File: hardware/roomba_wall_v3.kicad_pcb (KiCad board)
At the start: 2 copper layers, 27.9 x 26.7 mm, 15 parts, among them CON1 AVR-ISP-6, Q1 Q_NPN_BEC, SW1 Button, SW2 On/Off, U1 ATTINY45-20SU, Y1 8Mhz

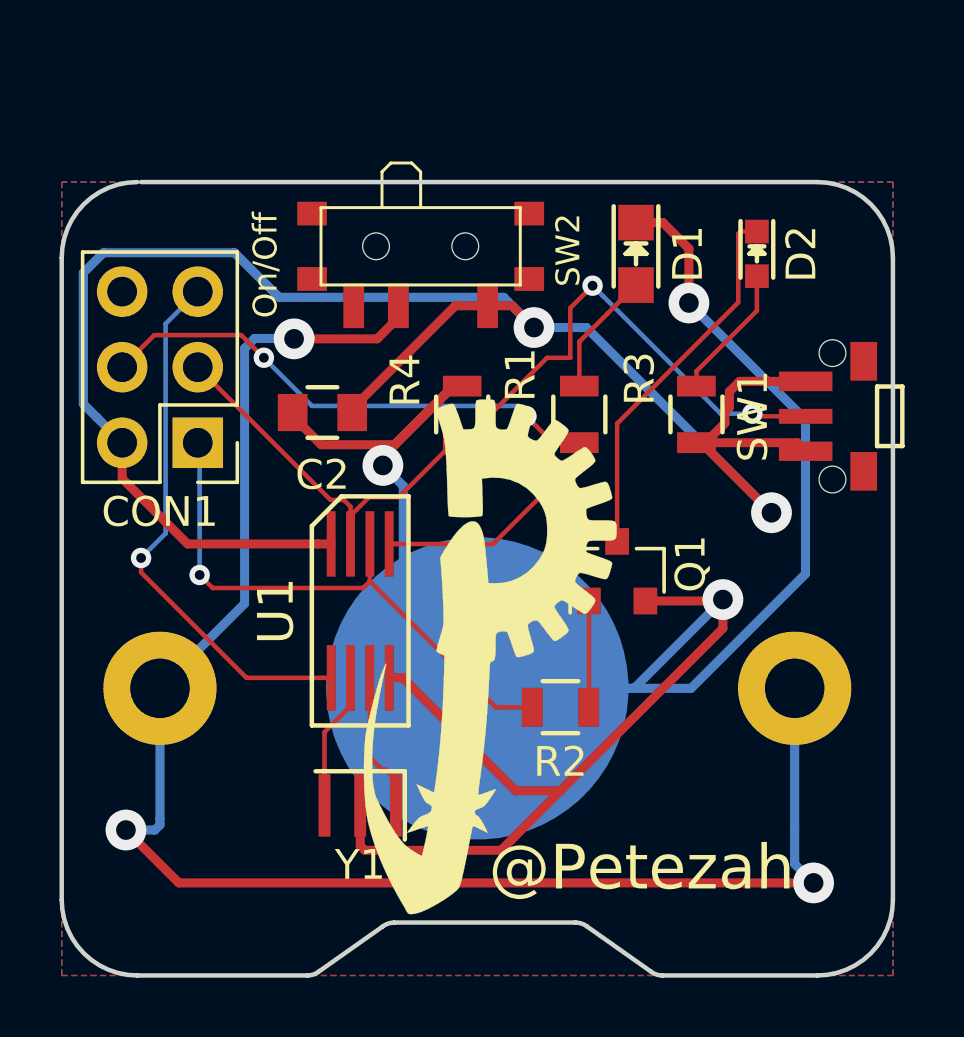
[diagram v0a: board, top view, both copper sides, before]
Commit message: Added a mounting hole for hanging and finalized layout for rev A Also exported gerbers
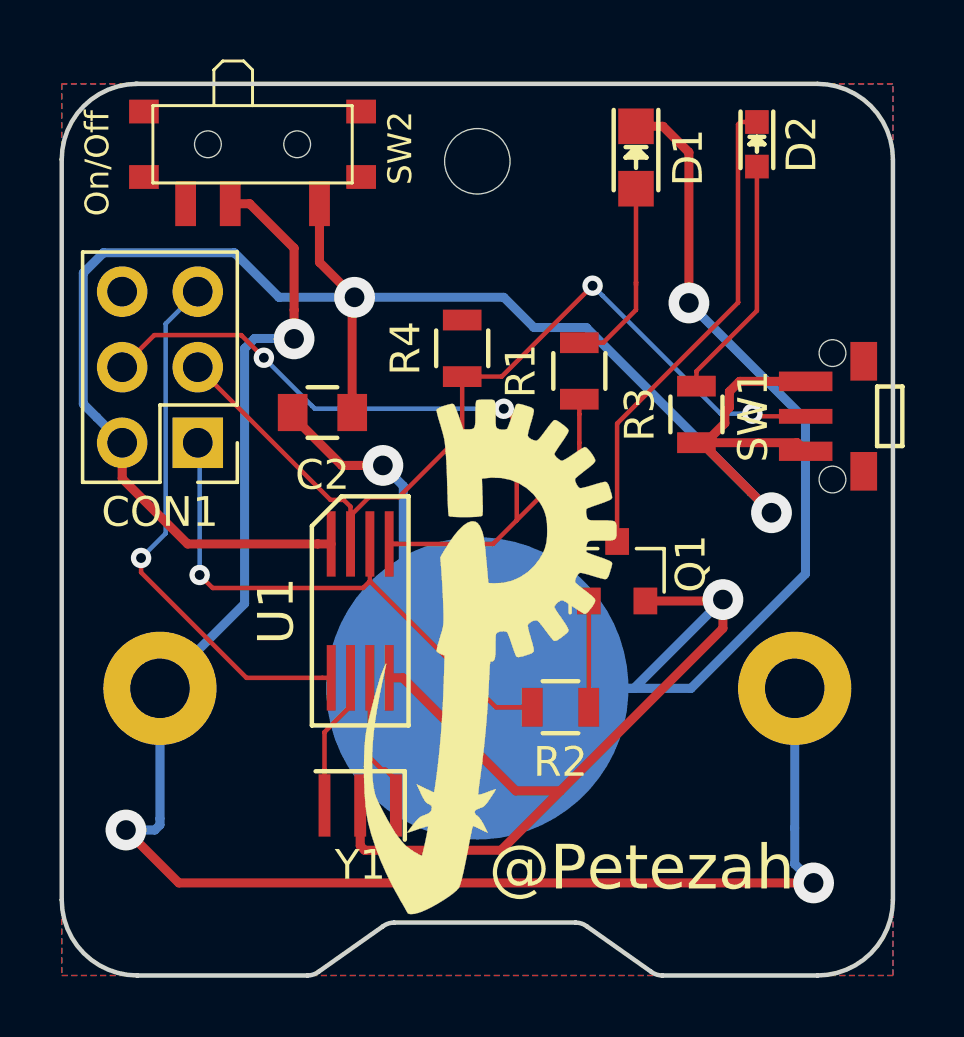
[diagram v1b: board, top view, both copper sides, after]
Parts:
- added REF**: MountingHole_2.2mm_M2, lib_fp:MountingHole_2.2mm_M2, F.Cu at (160.0, 107.3)
- moved SW2 6.61 mm to (152.5, 106.7)
- moved D2 3.68 mm to (169.4, 106.7)
- moved D1 3.24 mm to (165.4, 107.1)
- moved R4 2.22 mm to (159.5, 113.5)
- moved R1 1.46 mm to (163.4, 114.3)
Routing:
- net Net-(D2-Pad1): track 12.7 -> 16.4 mm
- net Net-(D2-Pad2): track 4.54 -> 8.22 mm
- net GND: track 83.9 -> 80.6 mm
- net Net-(D1-Pad2): track 4.19 -> 6.53 mm
- net /MOSI/INDICATOR: track 26.0 -> 28.1 mm
- net VBAT: track 55.1 -> 56.7 mm
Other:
- board size 27.9 x 26.7 mm -> 27.9 x 30 mm

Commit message: Working on rev B
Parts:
- removed SW2: On/Off, lib_fp:SSSS810701
- added G***: LOGO, kicad-libs:petezah-logo-xtiny, B.Cu at (148.1, 116.6)
- D2: footprint lib_fp:LED_0603 -> kicad-libs:VSMB3940X01-GS08
- moved CON1 9.12 mm to (155.0, 108.7), turned to 270 degrees
- moved D2 1.85 mm to (169.9, 108.5)
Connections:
- BT1 pad 1: VBAT -> +3V3
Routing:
- net GND: track 80.6 -> 1.03 mm, vias 3 -> 0
- net VBAT: track 56.7 -> 0.00 mm, vias 3 -> 0
- net +3V3: track 62.2 -> 39.2 mm, vias 2 -> 0
- net /RST: track 18.1 -> 32.0 mm, vias 1 -> 2
- net /MISO/IR: track 18.9 -> 27.0 mm
- net /MOSI/INDICATOR: track 28.1 -> 21.4 mm, vias 2 -> 1
- net Net-(D2-Pad2): track 8.22 -> 6.17 mm
- net Net-(D1-Pad2): track 6.53 -> 8.22 mm, vias 0 -> 2
- net Net-(D2-Pad1): track 16.4 -> 15.5 mm, vias 0 -> 2
- net /SCK/BUTTON: track 30.7 -> 31.6 mm
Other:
- net class 3V3: clearance 0.3048 -> 0.1524
- rule pad_to_mask_clearance: 0.2 -> 0.0508
- board text added: "Roomba Wall v3, Rev B (C) Copyright 2018 Peter Dunshee @Petezah"
- board text removed: "Roomba Wall v3, Rev A (C) Copyright 2018 Peter Dunshee @Petezah"

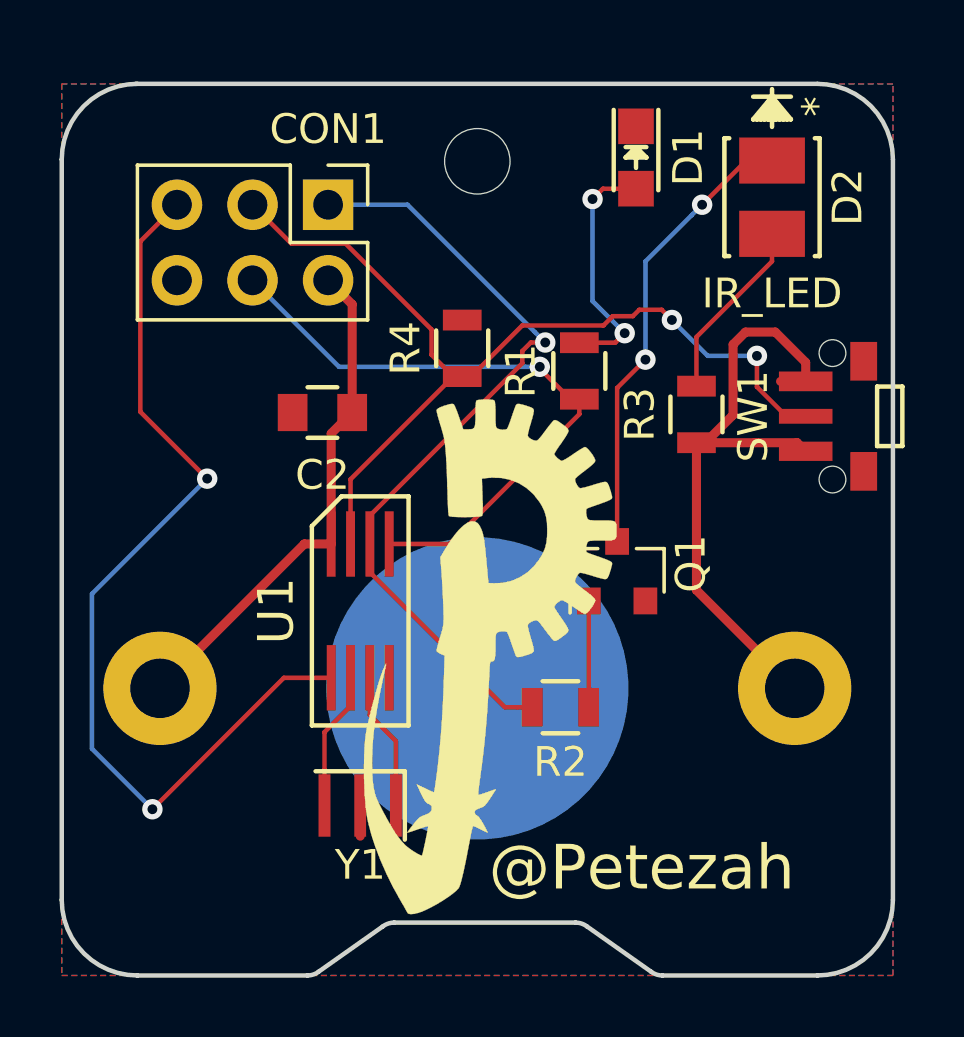
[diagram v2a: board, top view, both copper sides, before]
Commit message: Finished rev-b layout Updated gerbers Updated BOM Updated footprint archive Updated PDF schematic plot
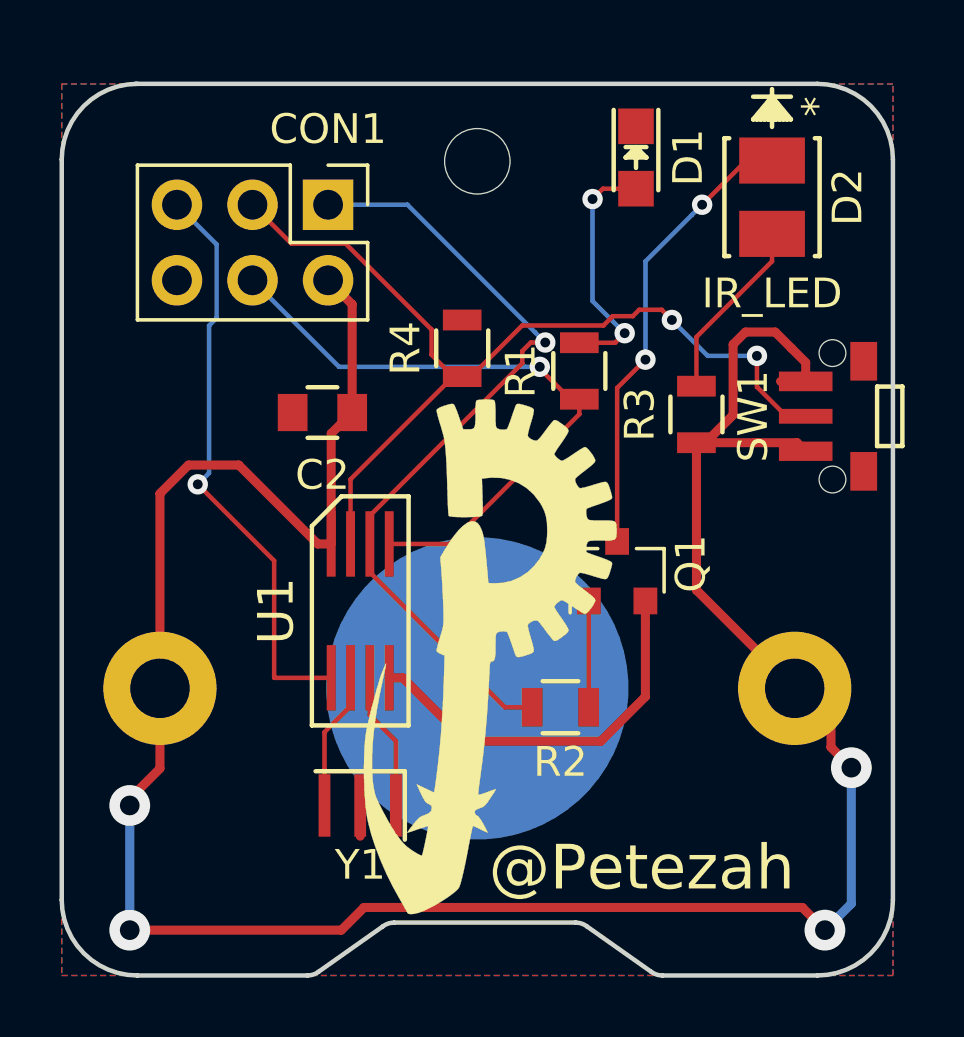
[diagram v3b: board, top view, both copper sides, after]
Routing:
- net +3V3: track 39.2 -> 87.0 mm, vias 0 -> 4
- net GND: track 1.03 -> 14.4 mm
- net /RST: track 32.0 -> 19.7 mm, vias 2 -> 1
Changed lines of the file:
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@@
-(kicad_pcb (version 4) (host pcbnew 4.0.6)
+(kicad_pcb (version 4) (host pcbnew 4.0.7)
   (general
     (links 28)
-    (no_connects 2)
-    (area 145.974999 104.572999 174.065001 134.695001)
+    (no_connects 0)
+    (area 144.267672 103.1241 176.2874 134.835901)
     (thickness 1.6)
     (drawings 18)
-    (tracks 106)
+    (tracks 134)
     (zones 0)
     (modules 16)
@@
   (gr_arc (start 148.59 132.08) (end 148.59 134.62) (angle 90) (layer Edge.Cuts) (width 0.15))
   (gr_arc (start 171.45 132.08) (end 173.99 132.08) (angle 90) (layer Edge.Cuts) (width 0.15))
+  (segment (start 159.766 126.746) (end 164.169642 126.746) (width 0.3048) (layer F.Cu) (net 1))
+  (segment (start 164.169642 126.746) (end 165.669 125.246642) (width 0.3048) (layer F.Cu) (net 1))
+  (segment (start 159.577801 126.557801) (end 159.766 126.746) (width 0.3048) (layer F.Cu) (net 1))
+  (segment (start 159.456101 126.557801) (end 159.577801 126.557801) (width 0.3048) (layer F.Cu) (net 1))
+  (segment (start 157.058 124.6145) (end 157.5128 124.6145) (width 0.3048) (layer F.Cu) (net 1))
+  (segment (start 157.5128 124.6145) (end 159.456101 126.557801) (width 0.3048) (layer F.Cu) (net 1))
+  (segment (start 165.669 122.7858) (end 165.669 122.031) (width 0.3048) (layer F.Cu) (net 1))
+  (segment (start 165.669 125.246642) (end 165.669 122.7858) (width 0.3048) (layer F.Cu) (net 1))
   (segment (start 156.083 129.938367) (end 156.083 128.905) (width 0.3048) (layer F.Cu) (net 1))
+  (segment (start 172.593 127.635) (end 171.907201 126.949201) (width 0.3048) (layer F.Cu) (net 2))
+  (segment (start 171.907201 126.949201) (end 171.907201 126.187201) (width 0.3048) (layer F.Cu) (net 2))
+  (segment (start 171.907201 126.187201) (end 170.688 124.968) (width 0.3048) (layer F.Cu) (net 2))
+  (segment (start 171.704 133.096) (end 172.593 132.207) (width 0.3048) (layer B.Cu) (net 2))
+  (segment (start 172.593 132.207) (end 172.593 127.635) (width 0.3048) (layer B.Cu) (net 2))
+  (via (at 172.593 127.635) (size 1.3716) (drill 0.6604) (layers F.Cu B.Cu) (net 2))
+  (segment (start 156.21 132.334) (end 170.942 132.334) (width 0.3048) (layer F.Cu) (net 2))
+  (segment (start 170.942 132.334) (end 171.704 133.096) (width 0.3048) (layer F.Cu) (net 2))
+  (via (at 171.704 133.096) (size 1.3716) (drill 0.6604) (layers F.Cu B.Cu) (net 2))
+  (segment (start 155.448 133.096) (end 156.21 132.334) (width 0.3048) (layer F.Cu) (net 2))
+  (segment (start 148.336 133.096) (end 155.448 133.096) (width 0.3048) (layer F.Cu) (net 2))
+  (segment (start 148.336 128.905) (end 148.336 133.096) (width 0.3048) (layer B.Cu) (net 2))
+  (via (at 148.336 133.096) (size 1.3716) (drill 0.6604) (layers F.Cu B.Cu) (net 2))
+  (segment (start 149.352 124.968) (end 149.352 127.662076) (width 0.3048) (layer F.Cu) (net 2))
+  (segment (start 149.352 127.662076) (end 148.336 128.678076) (width 0.3048) (layer F.Cu) (net 2))
+  (segment (start 148.336 128.678076) (end 148.336 128.905) (width 0.3048) (layer F.Cu) (net 2))
+  (via (at 148.336 128.905) (size 1.3716) (drill 0.6604) (layers F.Cu B.Cu) (net 2))
+  (segment (start 152.000998 117.462298) (end 154.6532 120.1145) (width 0.3048) (layer F.Cu) (net 2))
+  (segment (start 154.6532 120.1145) (end 155.108 120.1145) (width 0.3048) (layer F.Cu) (net 2))
+  (segment (start 150.311102 117.462298) (end 152.000998 117.462298) (width 0.3048) (layer F.Cu) (net 2))
+  (segment (start 149.352 118.4214) (end 150.311102 117.462298) (width 0.3048) (layer F.Cu) (net 2))
+  (segment (start 149.352 124.968) (end 149.352 118.4214) (width 0.3048) (layer F.Cu) (net 2))
+  (segment (start 171.058 114.0142) (end 170.5818 113.538) (width 0.3048) (layer F.Cu) (net 2))
+  (segment (start 170.5818 113.538) (end 170.035698 112.991898) (width 0.3048) (layer F.Cu) (net 2))
   (segment (start 168.617898 115.778602) (end 167.686 116.7105) (width 0.3048) (layer F.Cu) (net 2))
   (segment (start 167.686 116.7105) (end 167.386 116.7105) (width 0.3048) (layer F.Cu) (net 2))
@@
   (segment (start 169.3545 116.7105) (end 170.7695 116.7105) (width 0.3048) (layer F.Cu) (net 2))
   (segment (start 169.03395 112.991898) (end 168.617898 113.40795) (width 0.3048) (layer F.Cu) (net 2))
-  (segment (start 171.058 114.0142) (end 170.035698 112.991898) (width 0.3048) (layer F.Cu) (net 2))
   (segment (start 170.035698 112.991898) (end 169.03395 112.991898) (width 0.3048) (layer F.Cu) (net 2))
   (segment (start 171.058 114.649) (end 171.058 114.0142) (width 0.3048) (layer F.Cu) (net 2))
@@
   (segment (start 155.108 120.1145) (end 155.108 116.402) (width 0.3048) (layer F.Cu) (net 2))
   (segment (start 155.108 116.402) (end 155.813 115.697) (width 0.3048) (layer F.Cu) (net 2))
-  (segment (start 149.352 124.968) (end 154.2055 120.1145) (width 0.3048) (layer F.Cu) (net 2))
-  (segment (start 154.2055 120.1145) (end 155.108 120.1145) (width 0.3048) (layer F.Cu) (net 2))
   (segment (start 156.408 119.1645) (end 161.531311 114.041189) (width 0.1524) (layer F.Cu) (net 3))
   (segment (start 161.960789 113.00001) (end 162.303688 113.342909) (width 0.1524) (layer B.Cu) (net 3))
@@
   (segment (start 159.0869 120.1145) (end 163.449 115.7524) (width 0.1524) (layer F.Cu) (net 4))
   (segment (start 163.449 115.7524) (end 163.449 115.25) (width 0.1524) (layer F.Cu) (net 4))
-  (segment (start 149.098 129.032) (end 153.5155 124.6145) (width 0.1524) (layer F.Cu) (net 5))
-  (segment (start 153.5155 124.6145) (end 155.108 124.6145) (width 0.1524) (layer F.Cu) (net 5))
-  (segment (start 150.9395 117.9195) (end 147.065999 121.793001) (width 0.1524) (layer B.Cu) (net 5))
-  (segment (start 147.065999 121.793001) (end 147.065999 126.999999) (width 0.1524) (layer B.Cu) (net 5))
-  (segment (start 147.065999 126.999999) (end 149.098 129.032) (width 0.1524) (layer B.Cu) (net 5))
-  (via (at 149.098 129.032) (size 0.6858) (drill 0.3302) (layers F.Cu B.Cu) (net 5))
-  (segment (start 149.9235 108.712) (end 148.692499 109.943001) (width 0.1524) (layer F.Cu) (net 5))
-  (segment (start 148.692499 109.943001) (end 148.692499 115.672499) (width 0.1524) (layer F.Cu) (net 5))
-  (segment (start 148.692499 115.672499) (end 150.9395 117.9195) (width 0.1524) (layer F.Cu) (net 5))
-  (via (at 150.9395 117.9195) (size 0.6858) (drill 0.3302) (layers F.Cu B.Cu) (net 5))
+  (segment (start 150.622 118.11) (end 151.002101 117.729899) (width 0.1524) (layer B.Cu) (net 5))
+  (segment (start 151.002101 117.729899) (end 151.002101 112.776899) (width 0.1524) (layer B.Cu) (net 5))
+  (segment (start 151.002101 112.776899) (end 151.257 112.522) (width 0.1524) (layer B.Cu) (net 5))
+  (segment (start 151.257 112.522) (end 151.257 110.0455) (width 0.1524) (layer B.Cu) (net 5))
+  (segment (start 151.257 110.0455) (end 149.9235 108.712) (width 0.1524) (layer B.Cu) (net 5))
+  (segment (start 153.190997 124.6145) (end 153.190997 120.678997) (width 0.1524) (layer F.Cu) (net 5))
+  (via (at 150.622 118.11) (size 0.6858) (drill 0.3302) (layers F.Cu B.Cu) (net 5))
+  (segment (start 153.190997 120.678997) (end 150.622 118.11) (width 0.1524) (layer F.Cu) (net 5))
+  (segment (start 155.108 124.6145) (end 153.190997 124.6145) (width 0.1524) (layer F.Cu) (net 5))
   (segment (start 163.8935 108.5215) (end 164.24148 108.17352) (width 0.1524) (layer F.Cu) (net 6))
   (segment (start 164.24148 108.17352) (end 165.354 108.17352) (width 0.1524) (layer F.Cu) (net 6))
@@
     (min_thickness 0.254)
     (keepout (tracks not_allowed) (vias not_allowed) (copperpour allowed))
-    (fill (arc_segments 16) (thermal_gap 0.508) (thermal_bridge_width 0.508))
+    (fill yes (arc_segments 16) (thermal_gap 0.508) (thermal_bridge_width 0.508))
     (polygon
       (pts
